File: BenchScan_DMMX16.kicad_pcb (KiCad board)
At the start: 4 copper layers, 220 x 110 mm, 117 parts, among them J1 Phoenix 1190370 8POS, J10 POMONA 73099 BLACK, J11 POMONA 73099 RED, J12 POMONA 73099 BLACK, J2 Phoenix 1190370 8POS, J3 Phoenix 1190370 8POS, J4 Phoenix 1190370 8POS, J5 691137710006 DMM, J6 POMONA 73099 RED, J7 54-00129 BARREL 5V, J8 POMONA 73099 BLACK, J9 POMONA 73099 RED, K1 UD2-5NE, K10 UD2-5NE, K11 UD2-5NE, K12 UD2-5NE, K13 UD2-5NE, K14 UD2-5NE, K15 UD2-5NE, K16 UD2-5NE, K17 UD2-5NE, K2 UD2-5NE, K3 UD2-5NE, K4 UD2-5NE, K5 UD2-5NE, K6 UD2-5NE, K7 UD2-5NE, K8 UD2-5NE, K9 UD2-5NE, Q1 2N7002K, Q10 2N7002K, Q11 2N7002K, Q12 2N7002K, Q13 2N7002K, Q14 2N7002K, Q15 2N7002K, Q16 2N7002K, Q17 2N7002K, Q19 AO3401A, Q2 2N7002K, Q3 2N7002K, Q4 2N7002K, Q5 2N7002K, Q6 2N7002K, Q7 2N7002K, Q8 2N7002K, Q9 2N7002K, U1 XIAO ESP32-C6 / 113991254, U2 SN74HC595PWR, U3 SN74HC595PWR

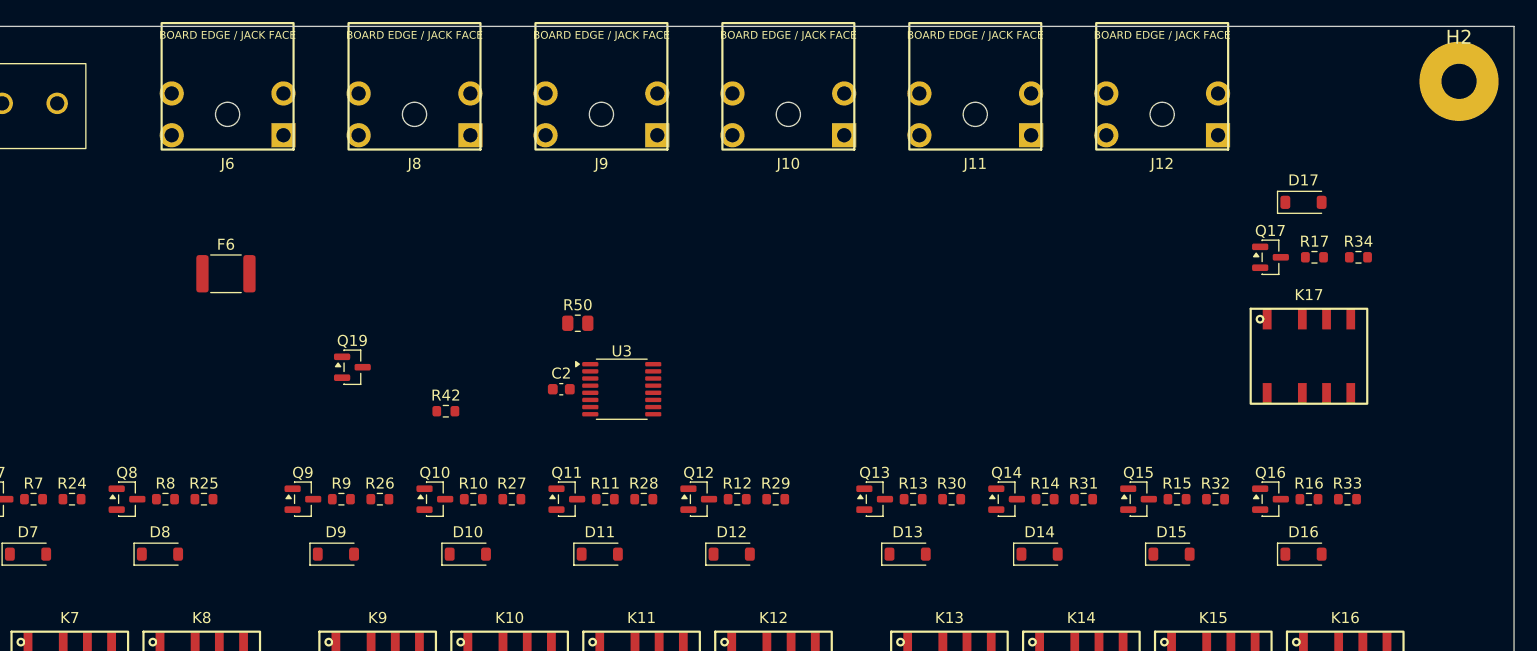
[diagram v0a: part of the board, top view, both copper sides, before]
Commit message: Correct Pomona 73099 connector footprints
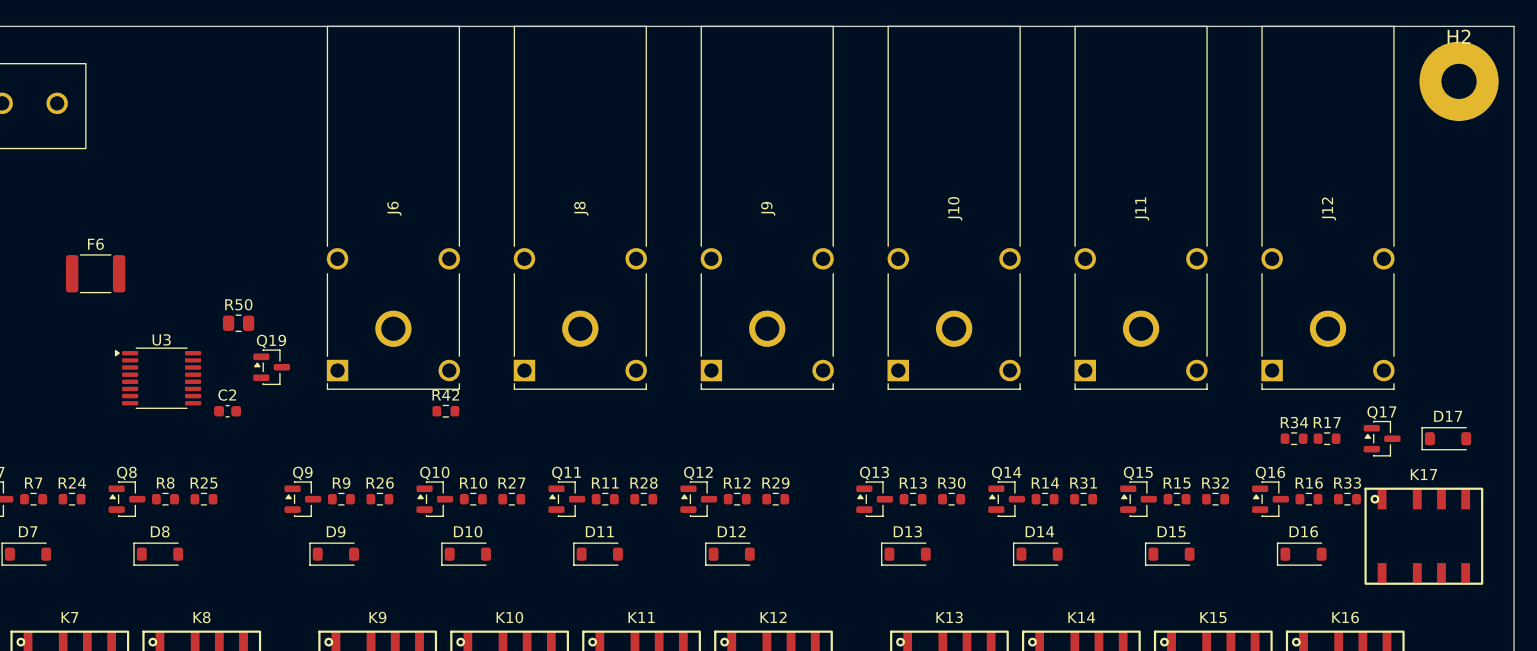
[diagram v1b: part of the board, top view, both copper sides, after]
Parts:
- moved U3 41.9 mm to (137.0, 64.0)
- moved R50 30.8 mm to (144.0, 59.0)
- moved C2 30.4 mm to (143.0, 67.0)
- moved J10 25.4 mm to (204.0, 63.3), turned to 90 degrees
- moved J11 25.4 mm to (221.0, 63.3), turned to 90 degrees
- moved J12 25.4 mm to (238.0, 63.3), turned to 90 degrees
- moved J6 25.4 mm to (153.0, 63.3), turned to 90 degrees
- moved J8 25.4 mm to (170.0, 63.3), turned to 90 degrees
- moved J9 25.4 mm to (187.0, 63.3), turned to 90 degrees
- moved D17 25.2 mm to (254.0, 69.5)
- moved K17 19.4 mm to (248.0, 75.0)
- moved Q17 19.4 mm to (248.0, 69.5)
- moved R34 17.5 mm to (240.0, 69.5)
- moved R17 16.5 mm to (243.0, 69.5)
- moved F6 11.8 mm to (131.0, 54.5)
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
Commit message: Refine PCB component placement
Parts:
- moved F4 15.4 mm to (231.0, 108.0), turned to 90 degrees
- moved F3 13.9 mm to (221.0, 108.0), turned to 90 degrees
- moved F2 12.0 mm to (211.5, 108.0), turned to 90 degrees
- moved F1 11.1 mm to (201.0, 108.0), turned to 90 degrees
- moved J1 5.39 mm to (63.0, 123.0)
- moved J2 5.39 mm to (109.0, 123.0)
- moved J3 5.39 mm to (155.0, 123.0)
- moved J4 5.39 mm to (201.0, 123.0)
- moved K3 4.07 mm to (74.7, 91.6)
- moved K4 4.07 mm to (86.7, 91.6)
- moved K5 4.07 mm to (102.7, 91.6)
- moved K6 4.07 mm to (114.7, 91.6)
- moved K7 4.07 mm to (126.7, 91.6)
- moved K1 4.07 mm to (50.7, 91.6)
- moved K2 4.07 mm to (62.7, 91.6)
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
